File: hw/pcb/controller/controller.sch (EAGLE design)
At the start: 0 parts

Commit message: Draft of schematic is complete
Still needs review.
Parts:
- added C1, C14: (no value), wedfestdress:CAP_GRM188R71E104KA01D
- added C10, C11, C16, C17, C18, C6, C9: (no value), wedfestdress:CAP_GRM185R61C105KE44D
- added C12, C13, C15, C2, C3: (no value), wedfestdress:CAP_C1608X7R1H104K080AA
- added C4, C5: (no value), wedfestdress:CAP_CL10B103KB8NNNC
- added C7, C8: (no value), wedfestdress:CAP_CGB3B1X5R1A475M055AC
- added D1, D2: (no value), wedfestdress:LED_LTST-C190GKT
- added D3: (no value), wedfestdress:LED_LS_Q976-NR-1
- added FB1: (no value), wedfestdress:FB_BK1608TS102-T
- added J1: (no value), wedfestdress:10118192-0001LF
- added J10: (no value), wedfestdress:MOLEX_5041950270
- added J11: (no value), wedfestdress:MOLEX_5041950370
- added J12: (no value), wedfestdress:DF13-3P-1.25H
- added J2: (no value), wedfestdress:MOLEX_0436500209
- added J3: (no value), wedfestdress:DF13-5P-1.25H
- added J4, J5, J6, J7, J8, J9: (no value), wedfestdress:MOLEX_5041950470
- added R1, R10, R11, R12, R13, R14, R15, R16, R17, R18, R19, R26, R6, R7, R8, R9: (no value), wedfestdress:RES_10K_RC0603FR-0710KL
- added R2: (no value), wedfestdress:RES_15K_RC0603FR-0715KL
- added R20, R29, R30, R31: (no value), wedfestdress:RES_1K_ERJ-3EKF1001V
- added R21, R24, R25: (no value), wedfestdress:RES_100K_RC0603FR-07100KL
- added R22, R23: (no value), wedfestdress:RES_2K2_ERJ-3EKF2201V
- added R27, R28: (no value), wedfestdress:RES_0R_RC0603JR-070RL
- added R3, R4: (no value), wedfestdress:RES_33R_RC0603FR-0733RL
- added R5: (no value), wedfestdress:RES_1K5_RC0603FR-071K5L
- added SW1, SW2, SW3: KMR221NG, wedfestdress:KMR221NG
- added SW4: CL-SB-22B-12T, wedfestdress:CL-SB-22B-12T
- added TP1, TP10, TP11, TP2, TP3, TP4, TP5, TP6, TP7, TP8, TP9: (no value), wedfestdress:TP_1P6_MM_ROUND
- added TVS1, TVS10, TVS11, TVS12, TVS13, TVS14, TVS15, TVS16, TVS17, TVS18, TVS19, TVS2, TVS20, TVS21, TVS22, TVS23, TVS24, TVS25, TVS26, TVS27, TVS3, TVS4, TVS5, TVS6, TVS7, TVS8, TVS9: (no value), wedfestdress:PESD5V0X1UB,135
- added U1: (no value), wedfestdress:LPC54114J256BD64
- added U10, U11, U12, U13, U14, U15, U4, U5, U6, U7, U8, U9: (no value), wedfestdress:SN74LVC1T45DCKR
- added U16, U17, U18, U19, U20, U3: (no value), wedfestdress:TPS27081
- added U2: (no value), wedfestdress:TCR2LF33,LM(CT
- added U21: (no value), wedfestdress:MCP6241UT-E/LT
- added U22: (no value), wedfestdress:MCP4017T
- added U23: (no value), wedfestdress:ADXL337
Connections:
- new net +6V: C9.P$1, J1.P$1, R1.P$2, TVS26.K
- new net 3V3: C11.P$1, C12.P$1, C13.P$2, C15.P$1, C2.P$1, C3.P$1, C4.P$1, C5.P$1, C6.P$1, C7.P$1, C8.P$1, FB1.P$1, J11.P2, J3.P1, R17.P$2, R19.P$2, R22.P$2, R23.P$2, R26.P$2, R5.P$2, R6.P$2, R7.P$1, R8.P$2, TP11.P1, TP5.P1, TP7.P1, TVS4.K, U1.VDD1, U1.VDD2, U1.VDD3, U1.VDD4, U10.DIR, U11.DIR, U12.DIR, U13.DIR, U14.DIR, U15.DIR, U2.OUT, U21.V+, U22.VDD, U23.VDD1, U23.VDD2, U4.DIR, U5.DIR, U6.DIR, U7.DIR, U8.DIR, U9.DIR
- new net ACCEL_TEST: TP1.P1, U23.ST
- new net ACCEL_XOUT: C18.P$1, U1.PIO1_0, U23.X
- new net ACCEL_YOUT: C17.P$1, U1.PIO1_1, U23.Y
- new net ACCEL_ZOUT: C16.P$1, U1.PIO1_2, U23.Z
- new net AUX_BTN: R26.P$1, SW3.P1, U1.PIO0_19
- new net BATT_DIV2: C14.P$1, R24.P$1, R25.P$2, U1.PIO1_4
- new net CLKOUT: TP6.P1, U1.PIO0_21
- new net FC0_MOSI: U1.PIO0_22, U4.A, U6.A, U8.A
- new net FC0_SCK: U1.PIO0_20, U5.A, U7.A, U9.A
- new net FC1_RXD: J12.P2, U1.PIO0_29
- new net FC1_TXD: J12.P3, U1.PIO0_30
- new net FC2_MOSI: U1.PIO0_8, U10.A, U12.A, U14.A
- new net FC2_SCK: U1.PIO0_10, U11.A, U13.A, U15.A
- new net FC5_SCL: R23.P$1, U1.PIO1_13, U22.SCL
- new net FC5_SDA: R22.P$1, U1.PIO1_12, U22.SDA
- new net FC6_RXD: TP3.P1, U1.PIO0_5
- new net FC6_TXD: TP2.P1, U1.PIO0_6
- new net GND: C1.P$2, C10.P$2, C11.P$2, C12.P$2, C13.P$1, C15.P$2, C16.P$2, C17.P$2, C18.P$2, C2.P$2, C3.P$2, C4.P$2, C5.P$2, C6.P$2, C7.P$2, C8.P$2, C9.P$2, J1.P$5, J10.P1, J11.P1, J12.P1, J2.P1, J3.P2, J4.P1, J5.P1, J6.P1, J7.P1, J8.P1, J9.P1, R16.P$1, R18.P$1, R2.P$1, R28.P$1, R29.P$1, R30.P$1, R31.P$1, SW1.P1, SW2.P2, SW3.P2, TP10.P1, TP4.P1, TP8.P1, TP9.P1, TVS1.A, TVS10.A, TVS11.A, TVS12.A, TVS13.A, TVS14.A, TVS15.A, TVS16.A, TVS17.A, TVS18.A, TVS19.A, TVS2.A, TVS20.A, TVS21.A, TVS22.A, TVS23.A, TVS24.A, TVS25.A, TVS26.A, TVS27.A, TVS3.A, TVS4.A, TVS5.A, TVS6.A, TVS7.A, TVS8.A, TVS9.A, U1.VREFN, U1.VSS1, U1.VSS2, U1.VSS3, U1.VSSA, U10.GND, U11.GND, U12.GND, U13.GND, U14.GND, U15.GND, U16.R2, U17.R2, U18.R2, U19.R2, U2.GND, U20.R2, U21.V-, U22.VSS, U23.GND1, U23.GND2, U3.R2, U4.GND, U5.GND, U6.GND, U7.GND, U8.GND, U9.GND
- new net GREEN_LED1: D1.A, U1.PIO0_14
- new net GREEN_LED2: D2.A, U1.PIO0_15
- new net ISP0: R8.P$1, SW2.P1, U1.PIO0_31
- new net ISP1: R7.P$2, U1.PIO0_4
- new net LED_PWR_EN: R16.P$2, U1.PIO0_2, U20.ON/OFF, U3.ON/OFF
- new net MIC_AMP_OUT: R21.P$2, U1.PIO1_3, U21.OUT, U22.W
- new net MIC_IN: J11.P3, R20.P$1
- new net N$1: R10.P$2, U3.R1/C1
- new net N$10: D3.K, R29.P$2
- new net N$11: D2.K, R30.P$2
- new net N$12: D1.K, R31.P$2
- new net N$16: R15.P$2, U20.R1/C1
- new net N$17: R11.P$2, U16.R1/C1
- new net N$19: R12.P$2, U17.R1/C1
- new net N$2: R3.P$2, U1.USB_DP
- new net N$21: R13.P$2, U18.R1/C1
- new net N$23: R14.P$2, U19.R1/C1
- new net N$3: R4.P$2, U1.USB_DM
- new net N$4: J1.P$2, R4.P$1, TVS2.K
- new net N$5: J1.P$3, R3.P$1, R5.P$1, TVS1.K
- new net N$6: R9.P$1, U2.EN
- new net N$7: R20.P$2, R21.P$1, U21.IN-, U22.B
- new net N$9: C14.P$2, R25.P$1, R27.P$1, R28.P$2
- new net RED_LED1: D3.A, U1.PIO0_18
- new net RESET_N: J3.P3, R6.P$1, SW1.P2, TVS5.K, U1.RESET
- new net STRING1_CLK: J4.P2, TVS23.K, U5.B
- new net STRING1_DATA: J4.P4, TVS25.K, U4.B
- new net STRING1_EN: U1.PIO0_23, U4.VCCA, U5.VCCA
- new net STRING1_V+: J4.P3, TVS24.K, U3.VOUT1, U3.VOUT2, U4.VCCB, U5.VCCB
- new net STRING2_CLK: J5.P2, TVS20.K, U7.B
- new net STRING2_DATA: J5.P4, TVS22.K, U6.B
- new net STRING2_EN: U1.PIO0_24, U6.VCCA, U7.VCCA
- new net STRING2_V+: J5.P3, TVS21.K, U16.VOUT1, U16.VOUT2, U6.VCCB, U7.VCCB
- new net STRING3_CLK: J6.P2, TVS17.K, U9.B
- new net STRING3_DATA: J6.P4, TVS19.K, U8.B
- new net STRING3_EN: U1.PIO0_25, U8.VCCA, U9.VCCA
- new net STRING3_V+: J6.P3, TVS18.K, U17.VOUT1, U17.VOUT2, U8.VCCB, U9.VCCB
- new net STRING4_CLK: J7.P2, TVS14.K, U11.B
- new net STRING4_DATA: J7.P4, TVS16.K, U10.B
- new net STRING4_EN: U1.PIO0_11, U10.VCCA, U11.VCCA
- new net STRING4_V+: J7.P3, TVS15.K, U10.VCCB, U11.VCCB, U18.VOUT1, U18.VOUT2
- new net STRING5_CLK: J8.P2, TVS11.K, U13.B
- new net STRING5_DATA: J8.P4, TVS13.K, U12.B
- new net STRING5_EN: U1.PIO0_12, U12.VCCA, U13.VCCA
- new net STRING5_V+: J8.P3, TVS12.K, U12.VCCB, U13.VCCB, U19.VOUT1, U19.VOUT2
- new net STRING6_CLK: J9.P2, TVS8.K, U15.B
- new net STRING6_DATA: J9.P4, TVS10.K, U14.B
- new net STRING6_EN: U1.PIO0_13, U14.VCCA, U15.VCCA
- new net STRING6_V+: J9.P3, TVS9.K, U14.VCCB, U15.VCCB, U20.VOUT1, U20.VOUT2
- new net SWCLK: J3.P4, TVS6.K, U1.SWCLK/PIO0_16
- new net SWDIO: J3.P5, TVS7.K, U1.SWDIO/PIO0_17
- new net USB_VBUS: R1.P$1, R2.P$2, U1.PIO1_6
- new net USER_BTN_IN: J10.P2, R17.P$1, U1.PIO1_17
- new net VBAT: J2.P2, R10.P$1, R11.P$1, R12.P$1, R13.P$1, R14.P$1, R15.P$1, R24.P$2, SW4.3, SW4.4, TVS27.K, U16.VIN, U17.VIN, U18.VIN, U19.VIN, U20.VIN, U3.VIN
- new net VBAT_READ_EN_R: R27.P$2, U1.PIO1_11
- new net VBAT_SW: C10.P$1, R9.P$2, SW4.5, SW4.6, TVS3.K, U2.VIN
- new net VDDA: C1.P$1, FB1.P$2, U1.VDDA, U1.VREFP
- new net VREF: R18.P$2, R19.P$1, U21.IN+
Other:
- note added: "A"
- note added: "Aux UART"
- note added: "Debug UART"
- note added: "ISP Enable"
- note added: "LED String 1"
- note added: "LED String 2"
- note added: "LED String 3"
- note added: "LED String 4"
- note added: "LED String 5"
- note added: "LED String 6"
- note added: "MCU Decoupling"
- note added: "Microphone Input"
- note added: "Programming Connector"
- note added: "User Button"
- note added: "Wedfestdress Controller"

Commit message: Routing and silscreen cleanup complete
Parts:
- removed R27, R28: (no value), wedfestdress:RES_0R_RC0603JR-070RL
- added TP12: (no value), wedfestdress:TP_1P6_MM_ROUND
- added TVS28, TVS29, TVS30: (no value), wedfestdress:PESD5V0X1UB,135
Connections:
- net N$7 renamed AMP_NEG
- removed net N$9: C14.P$2, R25.P$1, R27.P$1, R28.P$2
- removed net VBAT_READ_EN_R: R27.P$2, U1.PIO1_11
- net 3V3: now also TP12.P1, TVS29.K
- net GND: now also C14.P$2, R25.P$1, TVS28.A, TVS29.A, TVS30.A; no longer R28.P$1
- net LED_PWR_EN: now also U16.ON/OFF, U17.ON/OFF, U18.ON/OFF, U19.ON/OFF
- net MIC_IN: now also TVS30.K
- net STRING1_CLK: now also J4.P3; no longer J4.P2
- net STRING1_V+: now also J4.P2; no longer J4.P3
- net STRING2_CLK: now also J5.P3; no longer J5.P2
- net STRING2_V+: now also J5.P2; no longer J5.P3
- net STRING3_CLK: now also J6.P3; no longer J6.P2
- net STRING3_V+: now also J6.P2; no longer J6.P3
- net STRING4_CLK: now also J7.P3; no longer J7.P2
- net STRING4_V+: now also J7.P2; no longer J7.P3
- net STRING5_CLK: now also J8.P3; no longer J8.P2
- net STRING5_V+: now also J8.P2; no longer J8.P3
- net STRING6_CLK: now also J9.P3; no longer J9.P2
- net STRING6_V+: now also J9.P2; no longer J9.P3
- net USER_BTN_IN: now also TVS28.K
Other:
- moved on the sheet: C1, C10, C11, C12, C13, C15, C16, C17, C18, C2, C3, C4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

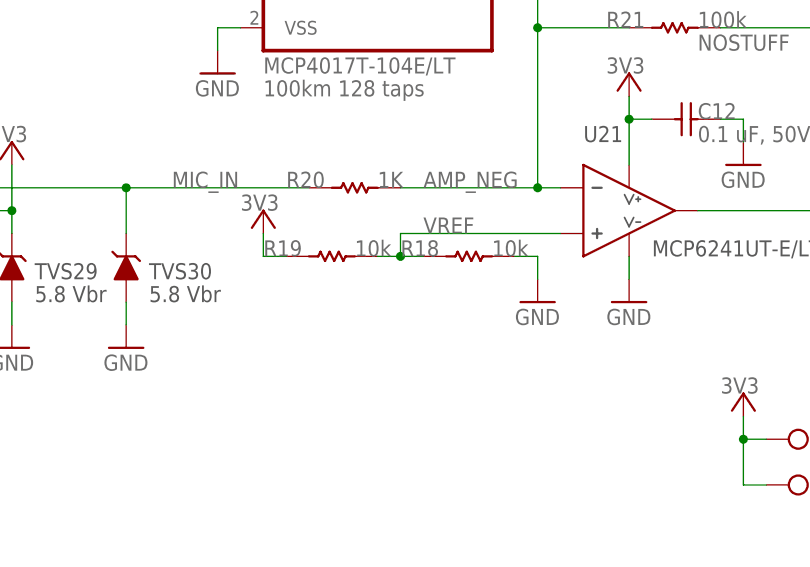
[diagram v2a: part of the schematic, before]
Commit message: Add microphone board
Completed schematic and layout of microphone board. Is a similar
design to the one from TI's tidu765 app-note. Has provisions for a
more basic non-inverting amplifier design as well. Currently uses a
transimpedence amplifier.
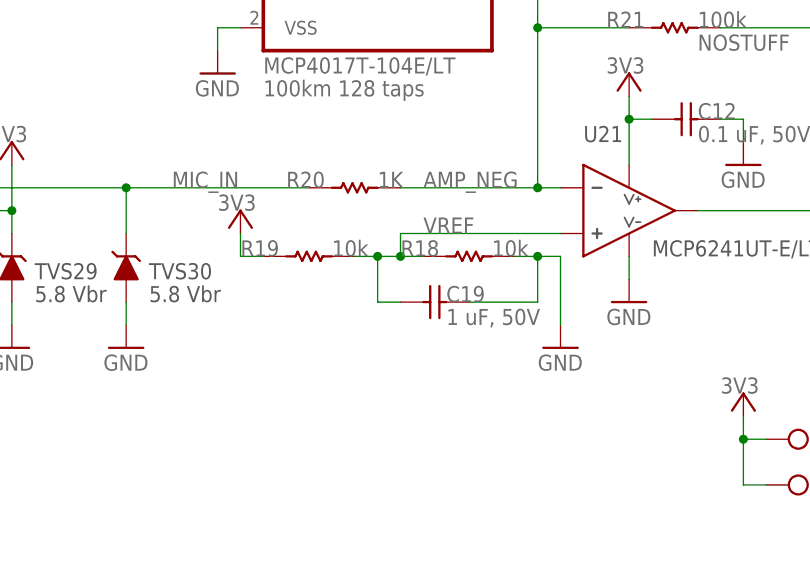
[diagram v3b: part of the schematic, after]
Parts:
- added C19: (no value), wedfestdress:CAP_GRM185R61C105KE44D
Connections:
- net GND: now also C19.P$2
- net VREF: now also C19.P$1
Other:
- moved on the sheet: R19
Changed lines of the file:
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@@
 <part name="GND41" library="wedfestdress" deviceset="GND" device=""/>
 <part name="GND42" library="wedfestdress" deviceset="GND" device=""/>
+<part name="C19" library="wedfestdress" deviceset="CAP_GRM185R61C105KE44D" device=""/>
 </parts>
 <sheets>
@@
 <attribute name="NOSTUFF" x="93.98" y="91.44" size="1.778" layer="96" rot="R180"/>
 </instance>
-<instance part="R19" gate="G$1" x="73.66" y="83.82" smashed="yes" rot="R180">
-<attribute name="VALUE" x="78.74" y="88.9" size="1.778" layer="96" rot="R180"/>
-<attribute name="NAME" x="66.04" y="83.82" size="1.778" layer="95"/>
-<attribute name="DISPLAY" x="76.2" y="83.82" size="1.778" layer="96"/>
-<attribute name="NOSTUFF" x="78.74" y="91.44" size="1.778" layer="96" rot="R180"/>
-</instance>
-<instance part="P+17" gate="1" x="66.04" y="88.9" smashed="yes">
-<attribute name="VALUE" x="63.5" y="88.9" size="1.778" layer="96"/>
-</instance>
-<instance part="GND26" gate="1" x="96.52" y="78.74"/>
+<instance part="R19" gate="G$1" x="71.12" y="83.82" smashed="yes" rot="R180">
+<attribute name="VALUE" x="76.2" y="88.9" size="1.778" layer="96" rot="R180"/>
+<attribute name="NAME" x="63.5" y="83.82" size="1.778" layer="95"/>
+<attribute name="DISPLAY" x="73.66" y="83.82" size="1.778" layer="96"/>
+<attribute name="NOSTUFF" x="76.2" y="91.44" size="1.778" layer="96" rot="R180"/>
+</instance>
+<instance part="P+17" gate="1" x="63.5" y="88.9" smashed="yes">
+<attribute name="VALUE" x="60.96" y="88.9" size="1.778" layer="96"/>
+</instance>
+<instance part="GND26" gate="1" x="99.06" y="73.66"/>
 <instance part="P+18" gate="1" x="106.68" y="104.14" smashed="yes">
 <attribute name="VALUE" x="104.14" y="104.14" size="1.778" layer="96"/>
@@
 <instance part="GND41" gate="1" x="38.1" y="73.66"/>
 <instance part="GND42" gate="1" x="50.8" y="73.66"/>
+<instance part="C19" gate="G$1" x="83.82" y="78.74" smashed="yes" rot="R90">
+<attribute name="VALUE" x="88.9" y="81.28" size="1.778" layer="96" rot="R90"/>
+<attribute name="DISPLAY" x="86.36" y="76.2" size="1.778" layer="96"/>
+<attribute name="NAME" x="86.36" y="78.74" size="1.778" layer="95"/>
+<attribute name="NOSTUFF" x="91.44" y="81.28" size="1.778" layer="96" rot="R90"/>
+</instance>
 </instances>
 <busses>
@@
 <pinref part="R18" gate="G$1" pin="P$1"/>
 <wire x1="93.98" y1="83.82" x2="96.52" y2="83.82" width="0.1524" layer="91"/>
-<wire x1="96.52" y1="83.82" x2="96.52" y2="81.28" width="0.1524" layer="91"/>
+<wire x1="96.52" y1="83.82" x2="99.06" y2="83.82" width="0.1524" layer="91"/>
+<wire x1="99.06" y1="83.82" x2="99.06" y2="76.2" width="0.1524" layer="91"/>
 <pinref part="GND26" gate="1" pin="GND"/>
+<pinref part="C19" gate="G$1" pin="P$2"/>
+<wire x1="88.9" y1="78.74" x2="96.52" y2="78.74" width="0.1524" layer="91"/>
+<wire x1="96.52" y1="78.74" x2="96.52" y2="83.82" width="0.1524" layer="91"/>
+<junction x="96.52" y="83.82"/>
 </segment>
 <segment>
@@
 <segment>
 <pinref part="P+17" gate="1" pin="3V3"/>
-<wire x1="66.04" y1="86.36" x2="66.04" y2="83.82" width="0.1524" layer="91"/>
+<wire x1="63.5" y1="86.36" x2="63.5" y2="83.82" width="0.1524" layer="91"/>
 <pinref part="R19" gate="G$1" pin="P$2"/>
-<wire x1="66.04" y1="83.82" x2="68.58" y2="83.82" width="0.1524" layer="91"/>
+<wire x1="63.5" y1="83.82" x2="66.04" y2="83.82" width="0.1524" layer="91"/>
 </segment>
 <segment>
@@
 <pinref part="R19" gate="G$1" pin="P$1"/>
 <pinref part="R18" gate="G$1" pin="P$2"/>
+<wire x1="76.2" y1="83.82" x2="78.74" y2="83.82" width="0.1524" layer="91"/>
 <wire x1="78.74" y1="83.82" x2="81.28" y2="83.82" width="0.1524" layer="91"/>
 <wire x1="81.28" y1="83.82" x2="83.82" y2="83.82" width="0.1524" layer="91"/>
@@
 <wire x1="81.28" y1="86.36" x2="99.06" y2="86.36" width="0.1524" layer="91"/>
 <label x="83.82" y="86.36" size="1.778" layer="95"/>
-</segment>
-</net>
+<pinref part="C19" gate="G$1" pin="P$1"/>
+<wire x1="81.28" y1="78.74" x2="78.74" y2="78.74" width="0.1524" layer="91"/>
+<wire x1="78.74" y1="78.74" x2="78.74" y2="83.82" width="0.1524" layer="91"/>
+<junction x="78.74" y="83.82"/>
+</segment>
+</net>
